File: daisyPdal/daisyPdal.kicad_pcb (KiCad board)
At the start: 2 copper layers, 3 parts, among them U1 L78L05_TO92

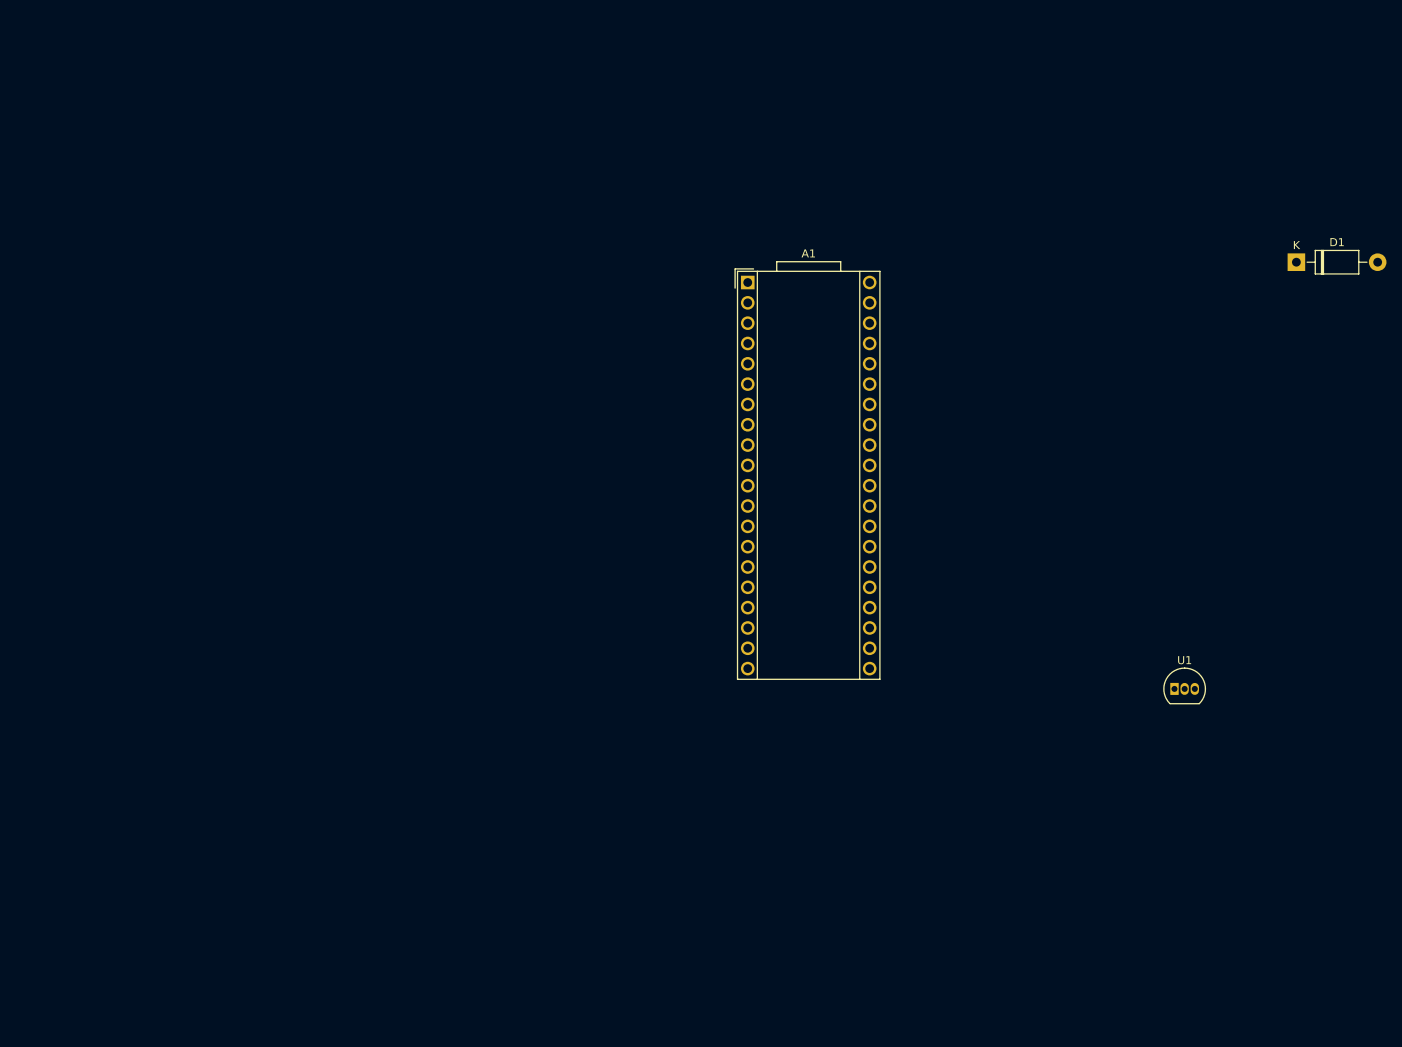
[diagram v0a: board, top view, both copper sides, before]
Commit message: Update schematic with pots, switches, encoder, LEDs
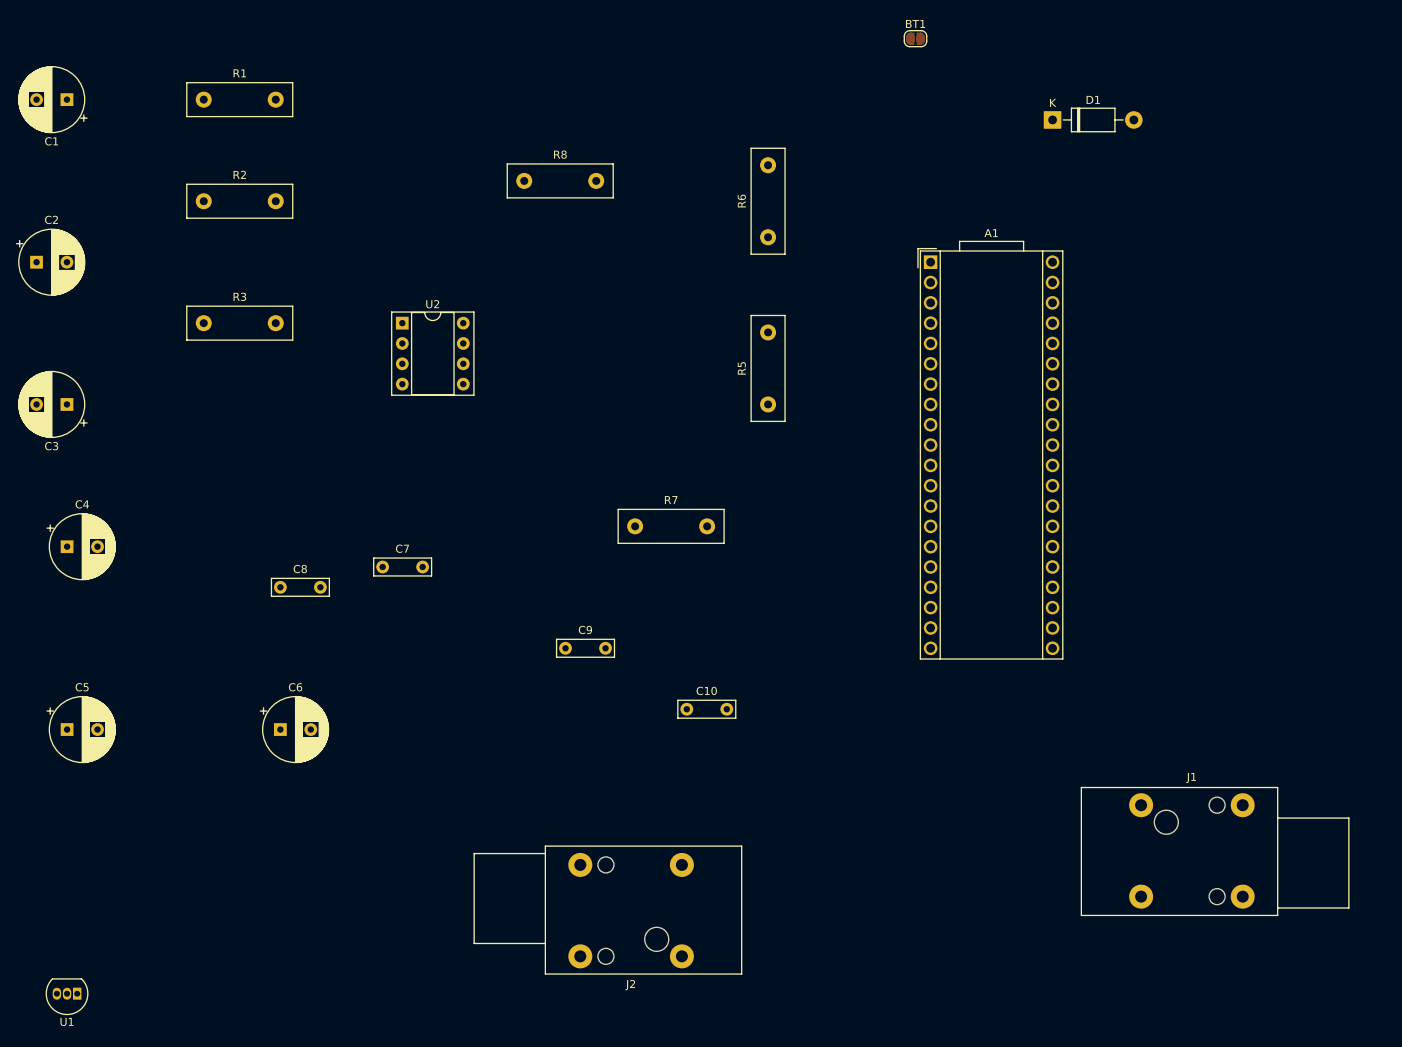
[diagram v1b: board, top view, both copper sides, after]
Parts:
- added BT1: Battery_Cell, Jumper:SolderJumper-2_P1.3mm_Open_RoundedPad1.0x1.5mm, F.Cu at (135.3, 20.3)
- added C1: 100n, Capacitor_THT:CP_Radial_D8.0mm_P3.80mm, F.Cu at (29.2, 27.9)
- added C10: 1u, Capacitor_THT:C_Rect_L7.0mm_W2.0mm_P5.00mm, F.Cu at (106.7, 104.1)
- added C2: 100u, Capacitor_THT:CP_Radial_D8.0mm_P3.80mm, F.Cu at (25.4, 48.3)
- added C3: 100n, Capacitor_THT:CP_Radial_D8.0mm_P3.80mm, F.Cu at (29.2, 66.0)
- added C4: 100n, Capacitor_THT:CP_Radial_D8.0mm_P3.80mm, F.Cu at (29.2, 83.8)
- added C5: 100n, Capacitor_THT:CP_Radial_D8.0mm_P3.80mm, F.Cu at (29.2, 106.7)
- added C6: 100p, Capacitor_THT:CP_Radial_D8.0mm_P3.80mm, F.Cu at (55.9, 106.7)
- added C7: 1n, Capacitor_THT:C_Rect_L7.0mm_W2.0mm_P5.00mm, F.Cu at (68.7, 86.4)
- added C8: 1u, Capacitor_THT:C_Rect_L7.0mm_W2.0mm_P5.00mm, F.Cu at (55.9, 88.9)
- added C9: 1u, Capacitor_THT:C_Rect_L7.0mm_W2.0mm_P5.00mm, F.Cu at (91.5, 96.5)
- added J1: AudioJack2, Connector_Audio:Jack_6.35mm_Neutrik_NRJ4HF_Horizontal, F.Cu at (163.5, 116.1)
- added J2: AudioJack2, Connector_Audio:Jack_6.35mm_Neutrik_NRJ4HF_Horizontal, F.Cu at (106.1, 135.0)
- added R1: 1M, Resistor_THT:R_Box_L13.0mm_W4.0mm_P9.00mm, F.Cu at (46.3, 27.9)
- added R2: 1M, Resistor_THT:R_Box_L13.0mm_W4.0mm_P9.00mm, F.Cu at (46.3, 40.6)
- added R3: 1k, Resistor_THT:R_Box_L13.0mm_W4.0mm_P9.00mm, F.Cu at (46.3, 55.9)
- added R5: 1M, Resistor_THT:R_Box_L13.0mm_W4.0mm_P9.00mm, F.Cu at (116.8, 66.0)
- added R6: 1M, Resistor_THT:R_Box_L13.0mm_W4.0mm_P9.00mm, F.Cu at (116.8, 45.1)
- added R7: 100K, Resistor_THT:R_Box_L13.0mm_W4.0mm_P9.00mm, F.Cu at (100.2, 81.3)
- added R8: 100R, Resistor_THT:R_Box_L13.0mm_W4.0mm_P9.00mm, F.Cu at (86.4, 38.1)
- added U2: TL072, Package_DIP:DIP-8_W7.62mm_Socket, F.Cu at (71.1, 55.9)
- moved U1 142.4 mm to (30.5, 139.7), turned to 180 degrees
- moved D1 35.3 mm to (152.4, 30.5)
- moved A1 23.0 mm to (137.2, 48.3)

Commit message: Lots of work on the schematic and PCB
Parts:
- added D2: LED 1, LED_THT:LED_D5.0mm-4_RGB, F.Cu at (132.7, 73.2)
- added D3: LED 2, LED_THT:LED_D5.0mm-4_RGB, F.Cu at (142.9, 73.5)
- added D4: LED, LED_THT:LED_D1.8mm_W3.3mm_H2.4mm, F.Cu at (136.7, 74.2)
- added J3: fsw pin 1, Connector_Wire:SolderWire-0.75sqmm_1x01_D1.25mm_OD3.5mm, F.Cu at (172.5, 52.0)
- added J4: fsw pin 4, Connector_Wire:SolderWire-0.75sqmm_1x01_D1.25mm_OD3.5mm, F.Cu at (172.5, 58.8)
- added J5: fsw pin 6, Connector_Wire:SolderWire-0.75sqmm_1x01_D1.25mm_OD3.5mm, F.Cu at (103.0, 61.8)
- added J6: fsw pin 3, Connector_Wire:SolderWire-0.75sqmm_1x01_D1.25mm_OD3.5mm, F.Cu at (159.8, 107.8)
- added J7: fsw pin 2, Connector_Wire:SolderWire-0.75sqmm_1x01_D1.25mm_OD3.5mm, F.Cu at (150.0, 66.2)
- added J8: fsw pin 5, Connector_Wire:SolderWire-0.75sqmm_1x01_D1.25mm_OD3.5mm, F.Cu at (161.2, 116.8)
- added R4: 1k, Resistor_THT:R_Axial_DIN0207_L6.3mm_D2.5mm_P10.16mm_Horizontal, F.Cu at (149.8, 50.5)
- added RV1: Knob 1, Potentiometer_THT:Potentiometer_Alps_RK09K_Single_Vertical, F.Cu at (114.7, 86.0)
- added RV2: Knob 2, Potentiometer_THT:Potentiometer_Alps_RK09K_Single_Vertical, F.Cu at (156.5, 85.8)
- added SW1: Switch 1, Button_Switch_THT:SW_CW_GPTS203211B_1 podal, F.Cu at (130.8, 86.0)
- added SW2: Switch 2, Button_Switch_THT:SW_CW_GPTS203211B_1 podal, F.Cu at (145.0, 86.0)
- added SW3: RotaryEncoder_Switch, Rotary_Encoder:RotaryEncoder_Alps_EC12E-Switch_Vertical_H20mm, F.Cu at (130.5, 57.8)
- BT1: footprint Jumper:SolderJumper-2_P1.3mm_Open_RoundedPad1.0x1.5mm -> Connector_BarrelJack:BarrelJack_Horizontal; moved to B.Cu
- C1, C3, C4, C5, C6: footprint Capacitor_THT:CP_Radial_D8.0mm_P3.80mm -> Capacitor_THT:C_Rect_L9.0mm_W2.5mm_P7.50mm_MKT
- C10, C7, C8, C9: footprint Capacitor_THT:C_Rect_L7.0mm_W2.0mm_P5.00mm -> Capacitor_THT:C_Rect_L9.0mm_W2.5mm_P7.50mm_MKT
- C2: footprint Capacitor_THT:CP_Radial_D8.0mm_P3.80mm -> Capacitor_THT:C_Radial_D10.0mm_H16.0mm_P5.00mm
- D1: footprint Diode_THT:D_DO-41_SOD81_P10.16mm_Horizontal -> Diode_THT:D_DO-41_SOD81_P7.62mm_Horizontal
- J1: value AudioJack2 -> Guitar in; footprint Connector_Audio:Jack_6.35mm_Neutrik_NRJ4HF_Horizontal -> Connector_Audio:Jack_6.35mm_Neutrik_NRJ6HM-1_Horizontal; moved to B.Cu
- J2: value AudioJack2 -> Left out; footprint Connector_Audio:Jack_6.35mm_Neutrik_NRJ4HF_Horizontal -> Connector_Audio:Jack_6.35mm_Neutrik_NRJ6HM-1_Horizontal; moved to B.Cu
- R1, R2, R3, R5, R6, R7, R8: footprint Resistor_THT:R_Box_L13.0mm_W4.0mm_P9.00mm -> Resistor_THT:R_Axial_DIN0207_L6.3mm_D2.5mm_P10.16mm_Horizontal
- moved C2 155.6 mm to (167.0, 112.8)
- moved U1 146.6 mm to (172.1, 102.0), turned to -90 degrees
- moved R1 134.9 mm to (155.2, 107.5), turned to -90 degrees
- moved R2 134.6 mm to (173.2, 85.5), turned to 90 degrees
- moved R3 126.6 mm to (168.8, 87.9), turned to -90 degrees
- moved C6 123.8 mm to (174.8, 72.0), turned to 180 degrees
- moved C8 113.5 mm to (168.8, 77.0), turned to -90 degrees
- moved C7 105.1 mm to (173.2, 96.2), turned to 90 degrees
- moved U2 98.9 mm to (163.6, 91.2), turned to -90 degrees
- moved R8 98.4 mm to (150.8, 112.5), turned to 180 degrees
- moved C1 95.7 mm to (107.0, 83.8), turned to 90 degrees
- moved C4 78.8 mm to (102.5, 112.8)
- moved J2 74.5 mm to (120.7, 62.0), turned to 90 degrees
- moved C3 74.3 mm to (102.8, 76.2), turned to -90 degrees
- moved C5 74.0 mm to (102.5, 117.0)
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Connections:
- A1 pad 14: unconnected-(A1-USART1_TX-Pad14) -> /ENC_CLICK
- A1 pad 21: unconnected-(A1-3V3_A-Pad21) -> /3v3
- A1 pad 22: unconnected-(A1-ADC_0-Pad22) -> Net-(A1-ADC_0)
- A1 pad 24: unconnected-(A1-ADC_2-Pad24) -> /LED_2_R
- A1 pad 25: unconnected-(A1-ADC_3-Pad25) -> /LED_1_B
- A1 pad 26: unconnected-(A1-ADC_4-Pad26) -> /LED_1_G
- A1 pad 27: unconnected-(A1-ADC_5-Pad27) -> /LED_1_R
- A1 pad 28: unconnected-(A1-ADC_6-Pad28) -> Net-(A1-ADC_6)
- A1 pad 30: unconnected-(A1-DAC_OUT1-Pad30) -> /LED_2_B
- A1 pad 31: unconnected-(A1-SAI2_MCLK-Pad31) -> /LED_2_G
- A1 pad 32: unconnected-(A1-SAI2_SD_B-Pad32) -> Net-(A1-SAI2_SD_B)
- A1 pad 33: unconnected-(A1-SAI2_SD_A-Pad33) -> Net-(A1-SAI2_SD_A)
- A1 pad 34: unconnected-(A1-SAI2_FS-Pad34) -> Net-(A1-SAI2_FS)
- A1 pad 35: unconnected-(A1-SAI2_SCK-Pad35) -> Net-(A1-SAI2_SCK)
- C6 pad 1: Net-(C6-Pad1) -> Net-(J4-Pin_1)
- C8 pad 1: Net-(C6-Pad1) -> Net-(J4-Pin_1)
- C9 pad 2: Net-(C9-Pad2) -> Net-(J6-Pin_1)
- J1 pad S: unconnected-(J1-PadS) -> GND
- J1 pad T: Net-(C6-Pad1) -> Net-(J3-Pin_1)
- J2 pad T: Net-(C9-Pad2) -> Net-(J5-Pin_1)
- R7 pad 1: Net-(C9-Pad2) -> Net-(J6-Pin_1)
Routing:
- net /VCC: track 0.00 -> 145.7 mm
- net +5V: track 0.00 -> 73.7 mm
- net /3v3: track 0.00 -> 60.5 mm, vias 0 -> 1
- net /LED_1_R: track 0.00 -> 56.2 mm
- net Net-(U2A-+): track 0.00 -> 55.2 mm
- net /ENC_CLICK: track 0.00 -> 51.2 mm
- net Net-(A1-SAI2_SD_A): track 0.00 -> 49.0 mm, vias 0 -> 1
- net Net-(U2B-+): track 0.00 -> 45.2 mm
- net /LED_1_B: track 0.00 -> 43.7 mm
- net Net-(J6-Pin_1): track 0.00 -> 37.1 mm
- net Net-(A1-SAI2_SCK): track 0.00 -> 34.1 mm
- net Net-(A1-SAI2_SD_B): track 0.00 -> 33.0 mm
- net /LED_1_G: track 0.00 -> 31.4 mm
- net GND: track 0.00 -> 30.3 mm, vias 0 -> 1
- net Net-(D4-K): track 0.00 -> 30.3 mm
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- added copper zone on B.Cu, net GND
- added copper zone on F.Cu, net GND
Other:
- board outline added: 76 x 80 mm

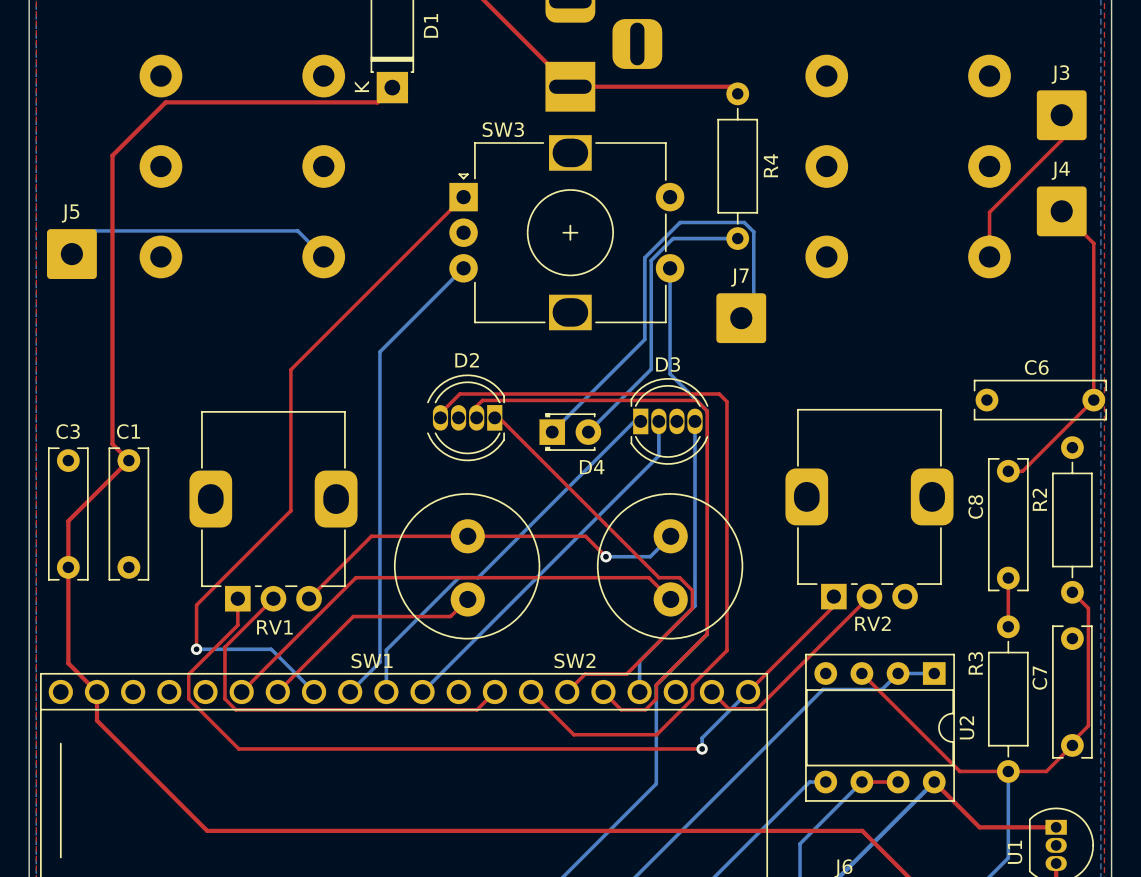
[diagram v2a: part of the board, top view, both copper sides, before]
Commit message: Move pots further apart; separate close traces
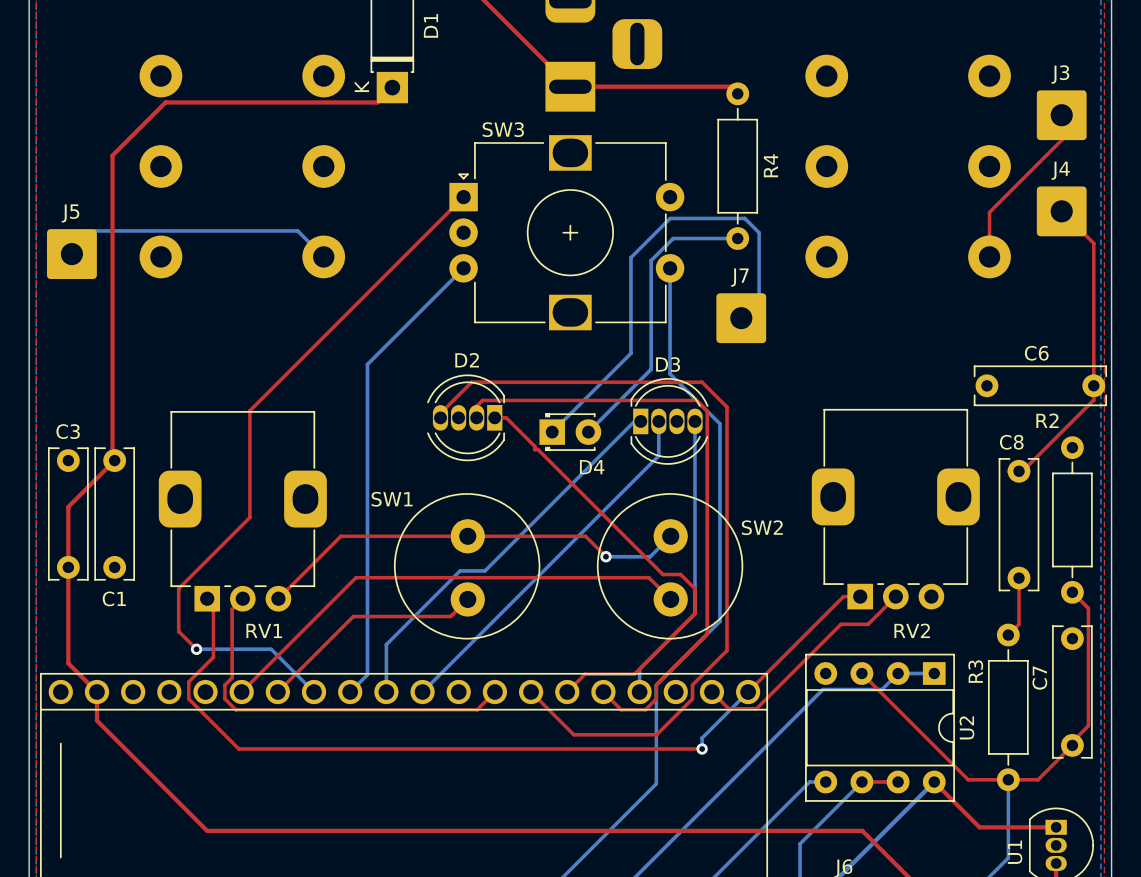
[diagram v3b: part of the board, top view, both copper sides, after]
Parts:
- moved RV1 2.15 mm to (112.5, 86.0)
- moved RV2 1.85 mm to (158.3, 85.8)
- moved C1 1.00 mm to (106.0, 83.8)
- moved C6 1.00 mm to (174.8, 71.0)
- moved C8 0.75 mm to (169.5, 77.0)
- moved R3 0.58 mm to (168.8, 88.5)
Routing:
- net GND: track 30.3 -> 32.5 mm
- net Net-(A1-ADC_0): track 14.8 -> 16.7 mm
- net Net-(D4-K): track 30.3 -> 31.6 mm
- net Net-(A1-SAI2_SD_A): track 49.0 -> 50.0 mm
- net /3v3: track 60.5 -> 61.4 mm
- net Net-(C8-Pad2): track 3.42 -> 4.31 mm
- net Net-(A1-ADC_6): track 28.2 -> 27.3 mm
- net /VCC: track 145.7 -> 144.8 mm
- net /LED_1_G: track 31.4 -> 32.2 mm
- net /ENC_CLICK: track 51.2 -> 51.9 mm
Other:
- board text added: "Podal v0.1"
